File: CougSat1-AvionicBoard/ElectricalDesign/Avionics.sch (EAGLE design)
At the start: 0 parts

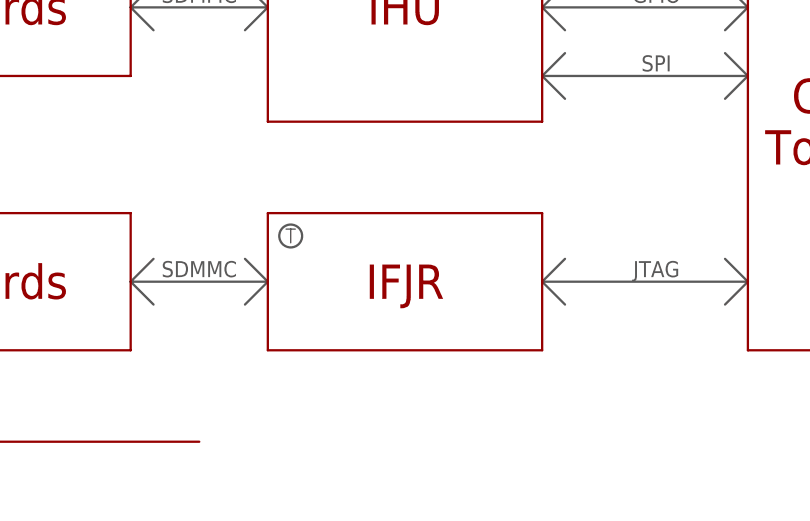
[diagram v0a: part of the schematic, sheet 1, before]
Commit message: Specified IFJR is a µController
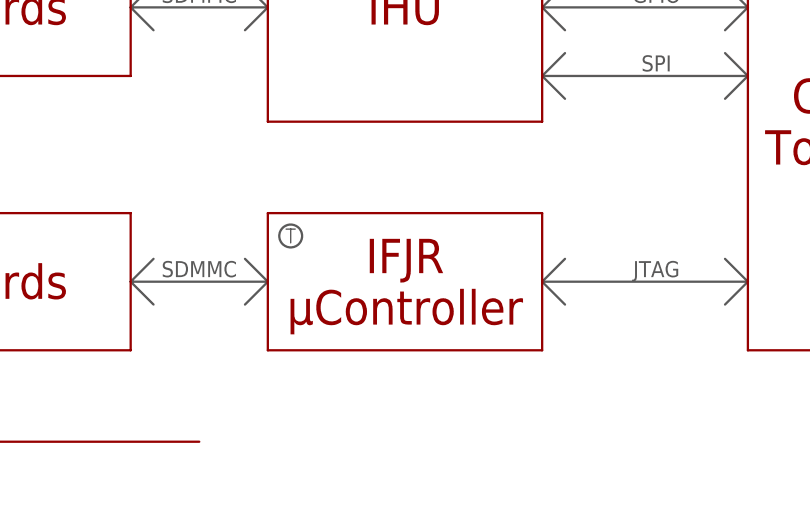
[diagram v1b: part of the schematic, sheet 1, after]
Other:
- note removed: "IFJR"
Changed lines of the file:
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@@
 <text x="215.9" y="60.96" size="3.81" layer="94" align="center">Connector:
 To Backplane</text>
-<text x="160.02" y="43.18" size="3.81" layer="94" align="center">IFJR</text>
+<text x="160.02" y="43.18" size="3.81" layer="94" align="center">IFJR
+µController</text>
 <text x="111.76" y="43.18" size="3.81" layer="94" align="center">SD Cards</text>
 <wire x1="198.12" y1="86.36" x2="233.68" y2="86.36" width="0.254" layer="94"/>

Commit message: Created Schematic for ADCS Portion
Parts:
- added C1, C2: 8pF ±0.25, CougsInSpace-Capacitors:CAP-V-8PF-1608
- added C10, C15: 1µF 10%, CougsInSpace-Capacitors:CAP-V-1UF-1608
- added C11, C12, C7, C8: 100nF 10%, CougsInSpace-Capacitors:CAP-V-100NF-1608
- added C13, C14: 15pF 1%, CougsInSpace-Capacitors:CAP-V-15PF-1608
- added C3: 10nF 10%, CougsInSpace-Capacitors:CAP-V-10NF-1608
- added C4: 10nF 10%, CougsInSpace-Capacitors:CAP-H-10NF-1608
- added C5: 100nF 10%, CougsInSpace-Capacitors:CAP-V-100NF-3216
- added C6: 6.8nF 5%, CougsInSpace-Capacitors:CAP-V-6.8NF-1608
- added D1: MBRM120LT, CougsInSpace-DiscreteSemi:DIODE-SCHOTTKY-H-POWERMITE
- added DS1: Green, CougsInSpace-LEDs:LED-V-GRN-1608
- added J1: (no value), CougsInSpace-Connectors:COAX-SMA-T-R
- added L1, L2, L3: xxx Turns, CougsInSpace-Coils:MAGNETORQUER-1UPV-SMD-3030
- added R1, R19, R2, R21, R3, R4: 0Ω <20mΩ, CougsInSpace-Resistors:RES-V-0-1608
- added R10, R11, R6, R7, R8, R9: 100mΩ 1%, CougsInSpace-Resistors:RES-H-0.1R-3216
- added R12, R14, R17: 33kΩ 1%, CougsInSpace-Resistors:RES-V-33K-1608
- added R13: 560Ω 1%, CougsInSpace-Resistors:RES-H-560R-1608
- added R15, R16: 8.45kΩ 0.1%, CougsInSpace-Resistors:RES-V-8.45K-1608
- added R18, R5: 0Ω <20mΩ, CougsInSpace-Resistors:RES-H-0-1608
- added R20, R22: 10kΩ 0.1%, CougsInSpace-Resistors:RES-V-10K-1608
- added RT1: 68kΩ 5%, CougsInSpace-Resistors:THERMISTOR-H-68K-1608
- added U10: BNO055, CougsInSpace-Sensors:BNO055
- added U2: STM32L476RGT, CougsInSpace-IC-µController:STM32-64P-L476RGT
- added U5, U6, U7: DRV8837, CougsInSpace-IC-Other:DRV8837
- added U8: LTC2499, CougsInSpace-IC-Conversion:LTC2499
- added U9: Venus838FLPx-L, CougsInSpace-RF:VENUS838FLPX
- added Y1: 16MHz ±10ppm, CougsInSpace-Clocks:CRYSTAL-16MHZ-SMD3.2X1.5
- added Y2: 32.768kHz ±10ppm, CougsInSpace-Clocks:CRYSTAL-32.768KHZ-SMD3.2X1.5
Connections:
- new net !NBOOT_LOAD_PIN: R22.2, U10.!BOOT_LOAD_PIN
- new net !NRESET: R20.1, U10.!RESET
- new net 3.3V: C7.1, U8.VCC
- new net 3.3V_2: C11.1, C12.1, D1.A, DS1.A, R12.2, U5.VCC, U6.VCC, U7.VCC, U9BASE.BOOT, U9BASE.VCC@1, U9BASE.VCC@2
- new net 5.0V: U5.VM, U6.VM, U7.VM
- new net ADCS_!WC: U2C.PC12
- new net ADCS_I2C_SCL: U2C.PC0, U8.SCL
- new net ADCS_I2C_SDA: U2C.PC1, U8.SDA
- new net ADCS_JDTO: U2B.PB3
- new net ADCS_JTCK: U2A.PA14
- new net ADCS_JTDI: U2A.PA15
- new net ADCS_JTMS: U2A.PA13
- new net AGND: J1.SHIELD, R15.2, R16.2, R2.1, R4.1, U8.COM, U8.REF-, U9BASE.RFGND
- new net AVDD: RT1.2
- new net AVREF: U8.REF+
- new net BUS_I2C0_IRQ: U2B.PB13
- new net BUS_I2C0_SCL: U2B.PB10
- new net BUS_I2C0_SDA: U2B.PB11
- new net CHASSIS: R3.1
- new net COIL-X_!SLEEP: U2B.PB4
- new net COIL-X_COIL+: L1.1, R7.2, U8.CH1
- new net COIL-X_IN1: U2B.PB9, U5.IN1
- new net COIL-X_IN2: U2B.PB8, U5.IN2
- new net COIL-X_OUT1: R6.1, U5.OUT1, U8.CH0
- new net COIL-X_SLEEP: U5.!SLEEP
- new net COIL-Y_!SLEEP: U2B.PB5
- new net COIL-Y_COIL+: L2.1, R9.2, U8.CH3
- new net COIL-Y_IN1: U2B.PB6, U6.IN1
- new net COIL-Y_IN2: U2B.PB7, U6.IN2
- new net COIL-Y_OUT1: R8.1, U6.OUT1, U8.CH2
- new net COIL-Y_SLEEP: U6.!SLEEP
- new net COIL-Z_!SLEEP: U2A.PA0
- new net COIL-Z_COIL+: L3.1, R11.2, U8.CH5
- new net COIL-Z_IN1: U2A.PA1, U7.IN1
- new net COIL-Z_IN2: U2A.PA2, U7.IN2
- new net COIL-Z_OUT1: R10.1, U7.OUT1, U8.CH4
- new net COIL-Z_SLEEP: U7.!SLEEP
- new net CTRL_RESET: R18.2
- new net DGND: C10.2, C11.2, C12.2, C13.2, C14.2, C15.2, C3.2, C4.1, C5.1, C6.2, C7.2, C8.2, R1.1, R20.2, R22.1, R5.1, U10.COM2, U10.DGND, U10.DGNDIO, U10.VDDIO, U2BASE.VSS@1, U2BASE.VSS@2, U2BASE.VSS@3, U2BASE.VSS@4, U2BASE.VSSA/VREF-, U8.CA0, U8.CA1, U8.CA2, U8.DGND, U8.F0, U9BASE.DGND, U9GPIO.GPIO1, U9GPIO.GPIO10, U9GPIO.GPIO11, U9GPIO.GPIO12, U9GPIO.GPIO13, U9GPIO.GPIO14, U9GPIO.GPIO15, U9GPIO.GPIO16, U9GPIO.GPIO2, U9GPIO.GPIO20, U9GPIO.GPIO21, U9GPIO.GPIO22, U9GPIO.GPIO23, U9GPIO.GPIO24, U9GPIO.GPIO25, U9GPIO.GPIO26, U9GPIO.GPIO27, U9GPIO.GPIO28, U9GPIO.GPIO29, U9GPIO.GPIO30, U9GPIO.GPIO31, U9GPIO.GPIO4, U9GPIO.GPIO5, U9GPIO.GPIO6, U9GPIO.GPIO7, U9GPIO.GPIO8, U9GPIO.GPIO9, Y1.GND
- new net GPS_!RESET: U2A.PA8
- new net GPS_LED: R13.1, U2B.PB12, U9BASE.LED
- new net GPS_PULSE: U2A.PA11, U9BASE.PULSE
- new net GPS_RESET: C10.1, R12.1, U9BASE.!RESET
- new net GPS_RX: U2A.PA10, U9BASE.TXD0
- new net GPS_TX: U2A.PA9, U9BASE.RXD0
- new net GPS_VBAT: C15.1, D1.C, U9BASE.VBAT
- new net I2C_ADDR_SEL: U10.COM3
- new net IMU_RESET: U2C.PC5
- new net INT: U10.INT
- new net N$1: C2.1, U2BASE.PH1-OSC_OUT, Y1.2
- new net N$10: R8.2, R9.1
- new net N$11: L2.2, U6.OUT2
- new net N$12: R10.2, R11.1
- new net N$13: R6.2, R7.1
- new net N$14: L3.2, U7.OUT2
- new net N$16: DS1.C, R13.2
- new net N$17: J1.CENTER, U9BASE.RFIN
- new net N$18: R16.1, R17.2, U8.ADCINP
- new net N$19: R14.1, U8.MUXOUTN
- new net N$2: C1.1, U2BASE.PH0-OSC_IN, Y1.1
- new net N$22: C13.1, U2C.PC14, Y2.1
- new net N$23: C14.1, U2C.PC15, Y2.2
- new net N$24: R17.1, U8.MUXOUTP
- new net N$25: R14.2, R15.1, U8.ADCINN
- new net N$27: U8.CH7
- new net N$28: U8.CH8
- new net N$3: R5.2, U2BASE.BOOT0
- new net N$4: C4.2, U10.CAP
- new net N$5: C1.2, C2.2
- new net N$6: C3.1, R18.1, U2BASE.!NRST
- new net N$8: C5.2, C6.1, C8.1, U10.VDD
- new net N$9: L1.2, U5.OUT2
- new net OPTIONAL_OSC_INPUT: U10.XIN32, U10.XOUT32
- new net PGND: R1.2, R2.2, R3.2, R4.2, U5.PGND, U6.PGND, U7.PGND
- new net PR_3.3V-2: U2BASE.VDD@1, U2BASE.VDD@2, U2BASE.VDD@3, U2BASE.VDDA/VREF+, U2BASE.VDDUSB
- new net PR_3.3V-3: R19.1, R21.1
- new net PS0: U10.PS0
- new net PS1: U10.PS1
- new net SCL: R19.2, U10.COM1
- new net SDA: R21.2, U10.COM0
- new net TEMP_GPS: RT1.1, U8.CH6
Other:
- note added: "3B1>"
- note added: "3B3>"
- note added: "5A2>"
- note added: "5A3>"
- note added: "5B2>"
- note added: "5B3>"
- note added: "5C2>"
- note added: "5C3>"
- note added: "6A2>"
- note added: "7B2>"
- note added: "7B3>"
- note added: "7C3>"
- note added: "<3B1"
- note added: "<3B4"
- note added: "<3B4>"
- note added: "<6B2"
- note added: "<7B3"
- note added: "<7C3"
- note added: "CAD Note: Decoupling"
- note added: "CAD Note: Thermally Connected"
- note removed: "SDMMC"

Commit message: Updated Avionics Schematic
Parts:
- added C16, C20, C21, C9: 8pF ±0.25, CougsInSpace-Capacitors:CAP-V-8PF-1608
- added C17, C18, C23, C24, C27, C28: 15pF 1%, CougsInSpace-Capacitors:CAP-V-15PF-1608
- added C19, C22: 10nF 10%, CougsInSpace-Capacitors:CAP-V-10NF-1608
- added C25, C26, C29, C30, C31: 100nF 10%, CougsInSpace-Capacitors:CAP-V-100NF-1608
- added J10, J16, J2, J6: (no value), CougsInSpace-Connectors:µSD-SW-PUSH-PUSH
- added J11, J12, J13, J14, J15, J5: (no value), CougsInSpace-Connectors:1X04-PICOLOCK
- added J3, J8, J9: SWD, CougsInSpace-Connectors:SWDSMD-6-R
- added J4, J7: CougSat Card, CougsInSpace-Boards:CIS_CARD-OPEN+X
- added R23, R24, R27, R28: 0Ω <20mΩ, CougsInSpace-Resistors:RES-H-0-1608
- added R25: 10kΩ 0.1%, CougsInSpace-Resistors:RES-V-10K-1608
- added R26, R36, R37, R38: 1kΩ 0.1%, CougsInSpace-Resistors:RES-V-1K-1608
- added R29, R30: 20kΩ 0.1%, CougsInSpace-Resistors:RES-V-PAIRED-20K-1616
- added R31: 20kΩ 0.1%, CougsInSpace-Resistors:RES-H-PAIRED-20K-1616
- added R33, R34, R35: 1kΩ 0.1%, CougsInSpace-Resistors:RES-H-1K-1608
- added RT2, RT3, RT4, RT5, RT6, RT7: 68kΩ 5%, CougsInSpace-Resistors:THERMISTOR-H-68K-1608
- added U1, U3: STM32L476RGT, CougsInSpace-IC-µController:STM32-64P-L476RGT
- added U11, U4: 128KB, CougsInSpace-IC-Memory:EEPROM-I2C-4-128KB-SO8
- added U12, U13: TXS0102DQM, CougsInSpace-IC-Logic:LEVEL_SHIFTER-2BIT-XSON-8
- added U14: LTC2499, CougsInSpace-IC-Conversion:LTC2499
- added Y3, Y5: 16MHz ±10ppm, CougsInSpace-Clocks:CRYSTAL-16MHZ-SMD3.2X1.5
- added Y4, Y6, Y7: 32.768kHz ±10ppm, CougsInSpace-Clocks:CRYSTAL-32.768KHZ-SMD3.2X1.5
- R14: value 33kΩ 1% -> 20kΩ 0.1%; device CougsInSpace-Resistors:RES-V-33K-1608 -> CougsInSpace-Resistors:RES-V-PAIRED-20K-1616
- R15: value 8.45kΩ 0.1% -> 20kΩ 0.1%; device CougsInSpace-Resistors:RES-V-8.45K-1608 -> CougsInSpace-Resistors:RES-V-PAIRED-20K-1616
- R16: value 8.45kΩ 0.1% -> 20kΩ 0.1%; device CougsInSpace-Resistors:RES-V-8.45K-1608 -> CougsInSpace-Resistors:RES-H-PAIRED-20K-1616
- R17: value 33kΩ 1% -> 20kΩ 0.1%; device CougsInSpace-Resistors:RES-V-33K-1608 -> CougsInSpace-Resistors:RES-H-PAIRED-20K-1616
- R19, R21: value 0Ω <20mΩ -> 1kΩ 0.1%; device CougsInSpace-Resistors:RES-V-0-1608 -> CougsInSpace-Resistors:RES-V-1K-1608
- R22: value 10kΩ 0.1% -> 1kΩ 0.1%; device CougsInSpace-Resistors:RES-V-10K-1608 -> CougsInSpace-Resistors:RES-V-1K-1608
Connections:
- net !NRESET renamed !IMU_RESET
- net INT renamed IMU0_INT
- net N$27 renamed TEMP_IMU
- removed net !NBOOT_LOAD_PIN: R22.2, U10.!BOOT_LOAD_PIN
- removed net 5.0V: U5.VM, U6.VM, U7.VM
- removed net ADCS_I2C_SCL: U2C.PC0, U8.SCL
- removed net ADCS_I2C_SDA: U2C.PC1, U8.SDA
- removed net I2C_ADDR_SEL: U10.COM3
- removed net OPTIONAL_OSC_INPUT: U10.XIN32, U10.XOUT32
- removed net PR_3.3V-2: U2BASE.VDD@1, U2BASE.VDD@2, U2BASE.VDD@3, U2BASE.VDDA/VREF+, U2BASE.VDDUSB
- removed net PR_3.3V-3: R19.1, R21.1
- removed net PS0: U10.PS0
- removed net PS1: U10.PS1
- removed net SCL: R19.2, U10.COM1
- removed net SDA: R21.2, U10.COM0
- new net !IMU0_BOOT-A: R25.2, U10.!BOOT_LOAD_PIN
- new net 3.3V_0: J7POWER.PR_3.3V-0, R35.2, R38.2, U3BASE.VBAT, U3BASE.VDD@1, U3BASE.VDD@2, U3BASE.VDD@3, U3BASE.VDDUSB
- new net 3.3V_1: J7POWER.PR_3.3V-1
- new net 3.3V_3: C5.2, C6.2, C8.2, R20.2, R25.1, U10.VDD, U10.VDDIO
- new net 3.3V_4: C11.1, C12.1, D1.A, DS1.A, R12.2, U9BASE.BOOT, U9BASE.VCC@1, U9BASE.VCC@2
- new net 3.3V_5: J10.VDD, J16.VDD, J2.VDD, J6.VDD, R34.2, R37.2, U12.VCCB, U13.VCCB
- new net 3.3V_6: C25.1, C26.1, C30.1, C31.1
- new net ADCS_!RESET: J3.!RST
- new net ADCS_I2C0_SCL: R26.1, U10.COM1, U11.SDA, U2B.PB6, U4.SDA, U8.SCL
- new net ADCS_I2C0_SDA: R22.1, U10.COM0, U11.SCL, U2B.PB7, U4.SCL, U8.SDA
- new net ADCS_I2C1_SCL: R21.1, U2C.PC0
- new net ADCS_I2C1_SDA: R19.1, U2C.PC1
- new net ADCS_JTDO: J3.SWO, U13.A1
- new net ADC_COIL-X_COIL+: R16.A2, U8.CH1
- new net ADC_COIL-X_OUT1: R16.B2, U8.CH0
- new net ADC_COIL-Y_COIL+: R17.A2, U8.CH3
- new net ADC_COIL-Y_OUT1: R17.B2, U8.CH2
- new net ADC_COIL-Z_COIL+: R31.A2, U8.CH5
- new net ADC_COIL-Z_OUT1: R31.B2, U8.CH4
- new net BUS_I2C1_IRQ: J4DATA.BUS_I2C1_IRQ, U3B.PB12
- new net BUS_I2C1_SCL: J4DATA.BUS_I2C1_SCL, U3B.PB13
- new net BUS_I2C1_SDA: J4DATA.BUS_I2C1_SDA, U3B.PB11
- new net BUS_JTAG_TCK: J4JTAG.BUS_JTAG_TCK, U12.B1, U1A.PA0
- new net BUS_JTAG_TDI: J4JTAG.BUS_JTAG_TDI, U12.B2, U1A.PA1
- new net BUS_JTAG_TDO: J4JTAG.BUS_JTAG_TDO, U13.B1, U1A.PA2
- new net BUS_JTAG_TMS: J4JTAG.BUS_JTAG_TMS, U13.B2, U1A.PA3
- new net CTRL_!RESET: J4DATA.CTRL_!RESET
- new net CTRL_SYNC: J4DATA.CTRL_SYNC
- new net EEPROM0_WC: U2C.PC6, U4.!WC
- new net EEPROM1_WC: U11.!WC, U2C.PC7
- new net I2C_SCL: J11.3, J12.3, J13.3, J14.3, J15.3, J5.3
- new net I2C_SDA: J11.2, J12.2, J13.2, J14.2, J15.2, J5.2
- new net IFJR_!RESET: J8.!RST
- new net IFJR_JDTI: U1A.PA15
- new net IFJR_JTCK: J8.SWCLK, U1A.PA14
- new net IFJR_JTDO: J8.SWO, U1B.PB3
- new net IFJR_JTMS: J8.SWDIO, U1A.PA13
- new net IHU_!RESET: J9.!RST
- new net IHU_GPIO-0: J4GPIO.GPIO-0, U3A.PA0
- new net IHU_GPIO-1: J4GPIO.GPIO-1, U3A.PA1
- new net IHU_GPIO-2: J4GPIO.GPIO-2, U3A.PA2
- new net IHU_GPIO-3: J4GPIO.GPIO-3, U3A.PA3
- new net IHU_GPIO-4: J4GPIO.GPIO-4, U3A.PA4
- new net IHU_GPIO-5: J4GPIO.GPIO-5, U3A.PA8
- new net IHU_GPIO-6: J4GPIO.GPIO-6, U3A.PA9
- new net IHU_GPIO-7: J4GPIO.GPIO-7, U3A.PA10
- new net IHU_GPIO-8: J4GPIO.GPIO-8, U3A.PA11
- new net IHU_GPIO-9: J4GPIO.GPIO-9, U3A.PA12
- new net IHU_JTCK: J9.SWCLK
- new net IHU_JTDO: J9.SWO
- new net IHU_JTMS: J9.SWDIO
- new net JTAG_OE: J4JTAG.BUS_JTAG_EN-0, U12.OE, U13.OE, U1C.PC3
- new net N$15: C16.1, U1BASE.PH1-OSC_OUT, Y3.2
- new net N$21: R23.2, U1BASE.BOOT0
- new net N$26: C17.1, U1C.PC14, Y4.1
- new net N$27: R29.B2, U14.MUXOUTN
- new net N$29: C18.1, U1C.PC15, Y4.2
- new net N$30: C19.1, R24.1, U1BASE.!NRST
- new net N$31: C20.2, C21.2
- new net N$32: R27.2, U3BASE.BOOT0
- new net N$33: J16.CD/DAT3
- new net N$34: C20.1, U3BASE.PH0-OSC_IN, Y5.1
- new net N$35: C22.1, R28.1, U3BASE.!NRST
- new net N$36: C23.1, U3C.PC14, Y6.1
- new net N$37: C27.1, U10.XOUT32, Y7.1
- new net N$38: C24.1, U3C.PC15, Y6.2
- new net N$39: C4.1
- new net N$40: J6.CD/DAT3
- new net N$41: J2.CMD, J6.CMD
- new net N$42: U1BASE.VBAT, U1BASE.VDD@1, U1BASE.VDD@2, U1BASE.VDD@3, U1BASE.VDDUSB
- new net N$43: J2.CLK, J6.CLK
- new net N$44: C28.1, U10.XIN32, Y7.2
- new net N$45: J2.DAT0, J6.DAT0
- new net N$46: J6.SW+
- new net N$47: J2.CD/DAT3
- new net N$50: J2.SW+
- new net N$51: R29.B1, R30.B2, U14.ADCINN
- new net N$52: J7POWER.PR_3.3V-3
- new net N$53: J7POWER.PR_3.3V-4
- new net N$54: J7POWER.PR_3.3V-5
- new net N$55: J10.CMD, J16.CMD
- new net N$56: J10.CLK, J16.CLK
- new net N$57: J10.DAT0, J16.DAT0
- new net N$58: R33.1, U2BASE.VDDA/VREF+
- new net N$59: R34.1, U1BASE.VDDA/VREF+
- new net N$60: R35.1, U3BASE.VDDA/VREF+
- new net N$61: J3.VSENSE, R36.1
- new net N$62: J8.VSENSE, R37.1
- new net N$64: J9.VSENSE, R38.1
- new net N$65: R29.A1, R30.A2, U14.ADCINP
- new net N$7: C21.1, U3BASE.PH1-OSC_OUT, Y5.2
- new net N$70: J16.SW+
- new net N$71: J10.CD/DAT3
- new net N$72: J10.SW+
- new net SPI1_MISO: J4DATA.BUS_SPI_MISO, U1A.PA6, U3A.PA6
- new net SPI1_MOSI: J4DATA.BUS_SPI_MOSI, U1A.PA7, U3A.PA7
- new net SPI1_SCK: J4DATA.BUS_SPI_SCK, U1A.PA5, U3A.PA5
- new net SPI2_MISO: U3C.PC2
- new net SPI2_MOSI: U3C.PC3
- new net SPI2_SCK: U3B.PB10
- new net SPI3_MISO: U3C.PC11
- new net SPI3_MOSI: U3C.PC12
- new net SPI3_SCK: U3C.PC10
- new net SYS_JTCK-SWCLK: U3A.PA14
- new net SYS_JTDI: U3A.PA15
- new net SYS_JTDO-SWO: U3B.PB3
- new net SYS_JTMS-SWDIO: U3A.PA13
- new net TEMP_ADCS: U8.CH9
- new net TEMP_H-BRIDGE-X: RT3.1, U8.CH10
- new net TEMP_H-BRIDGE-Y: RT4.1, U8.CH11
- new net TEMP_H-BRIDGE-Z: RT5.1, U8.CH12
- new net TEMP_IFJR: RT2.1, U14.CH1
- new net TEMP_IHU: U14.CH0
- new net TEMP_SD_IFJR0: RT6.1, U14.CH4
- new net TEMP_SD_IFJR1: RT7.1, U14.CH5
- new net TEMP_SD_IHU0: U14.CH2
- new net TEMP_SD_IHU1: U14.CH3
- new net VBATT_5: J7POWER.PR_BATT-5, U5.VM, U6.VM, U7.VM
- net 3.3V: now also C29.1, J11.1, J12.1, J13.1, J14.1, J15.1, J5.1, U14.VCC
- net 3.3V_2: now also J7POWER.PR_3.3V-2, R33.2, R36.2, U11.E1, U11.VCC, U12.VCCA, U13.VCCA, U2BASE.VBAT, U2BASE.VDD@1, U2BASE.VDD@2, U2BASE.VDD@3, U2BASE.VDDUSB, U4.VCC; no longer C11.1, C12.1, D1.A, DS1.A, R12.2, U9BASE.BOOT, U9BASE.VCC@1, U9BASE.VCC@2
- net ADCS_!WC: now also U2C.PC4; no longer U2C.PC12
- net ADCS_JTCK: now also J3.SWCLK, U12.A1
- net ADCS_JTDI: now also U12.A2
- net ADCS_JTMS: now also J3.SWDIO, U13.A2
- net AGND: now also R15.A1, R15.B1, R30.A1, R30.B1, U14.COM, U14.REF-; no longer R15.2, R16.2
- net AVDD: now also RT2.2, RT3.2, RT4.2, RT5.2, RT6.2, RT7.2, U14.REF+, U8.REF+
- net AVREF: now also U14.CH8, U8.CH8; no longer U8.REF+
- net BUS_I2C0_IRQ: now also J4DATA.BUS_I2C0_IRQ, U2B.PB12, U3B.PB8; no longer U2B.PB13
- net BUS_I2C0_SCL: now also J4DATA.BUS_I2C0_SCL, U3B.PB6
- net BUS_I2C0_SDA: now also J4DATA.BUS_I2C0_SDA, U3B.PB7
- net CHASSIS: now also J7POWER.CHASSIS
- net COIL-X_!SLEEP: now also U2A.PA4; no longer U2B.PB4
- net COIL-X_COIL+: now also R16.A1; no longer U8.CH1
- net COIL-X_IN1: now also U2A.PA0; no longer U2B.PB9
- net COIL-X_IN2: now also U2A.PA1; no longer U2B.PB8
- net COIL-X_OUT1: now also R16.B1; no longer U8.CH0
- net COIL-Y_!SLEEP: now also U2A.PA5; no longer U2B.PB5
- net COIL-Y_COIL+: now also R17.A1; no longer U8.CH3
- net COIL-Y_IN1: now also U2A.PA2; no longer U2B.PB6
- net COIL-Y_IN2: now also U2A.PA3; no longer U2B.PB7
- net COIL-Y_OUT1: now also R17.B1; no longer U8.CH2
- net COIL-Z_!SLEEP: now also U2A.PA12; no longer U2A.PA0
- net COIL-Z_COIL+: now also R31.A1; no longer U8.CH5
- net COIL-Z_IN1: now also U2A.PA8; no longer U2A.PA1
- net COIL-Z_IN2: now also U2A.PA11; no longer U2A.PA2
- net COIL-Z_OUT1: now also R31.B1; no longer U8.CH4
- net CTRL_RESET: now also R24.2, R28.2
- net DGND: now also C16.2, C17.2, C18.2, C19.2, C22.2, C23.2, C24.2, C25.2, C26.2, C27.2, C28.2, C29.2, C30.2, C31.2, C6.1, C8.1, C9.2, J10.SW-, J10.VSS, J11.4, J12.4, J13.4, J14.4, J15.4, J16.SW-, J16.VSS, J2.SW-, J2.VSS, J3.DGND, J5.4, J6.SW-, J6.VSS, J8.DGND, J9.DGND, R23.1, R27.1, U10.COM3, U10.PS0, U10.PS1, U11.DGND, U11.E2, U12.DGND, U13.DGND, U14.CA0, U14.CA1, U14.CA2, U14.DGND, U14.F0, U1BASE.VSS@1, U1BASE.VSS@2, U1BASE.VSS@3, U1BASE.VSS@4, U1BASE.VSSA/VREF-, U3BASE.VSS@1, U3BASE.VSS@2, U3BASE.VSS@3, U3BASE.VSS@4, U3BASE.VSSA/VREF-, U4.DGND, U4.E1, U4.E2, Y3.GND, Y5.GND; no longer C4.1, C6.2, C8.2, R20.2, R22.1, U10.VDDIO
- net GPS_!RESET: now also U2A.PA6; no longer U2A.PA8
- net GPS_LED: now also U2B.PB0; no longer U2B.PB12
- net GPS_PULSE: now also U2A.PA7; no longer U2A.PA11
- net IMU_RESET: now also U2C.PC3; no longer U2C.PC5
- net N$18: now also R14.B1, R15.B2, U8.ADCINN; no longer R16.1, R17.2, U8.ADCINP
- net N$19: now also R14.A1, R15.A2, U8.ADCINP; no longer R14.1, U8.MUXOUTN
- net N$22: no longer U2C.PC14
- net N$24: now also R14.B2, U8.MUXOUTN; no longer R17.1, U8.MUXOUTP
- net N$25: now also R14.A2, U8.MUXOUTP; no longer R14.2, R15.1, U8.ADCINN
- net N$28: now also R29.A2, U14.MUXOUTP; no longer U8.CH8
- net N$8: now also C9.1, U1BASE.PH0-OSC_IN, Y3.1; no longer C5.2, C6.1, C8.1, U10.VDD
- net PGND: now also J7POWER.PGND
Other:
- note added: "3B2>"
- note added: "3B6>"
- note added: "3C2> 3D2>"
- note added: "5A1>"
- note added: "5B1>"
- note added: "5C1>"
- note added: "7B1>"
- note added: "<3B2"
- note added: "<3B3"
- note added: "<3B3>"
- note added: "<3B6"
- note added: "<3B6>"
- note added: "<3C1"
- note removed: "3B1>"
- note removed: "5A2>"
- note removed: "5A3>"
- note removed: "5B2>"
- note removed: "5B3>"
- note removed: "5C2>"
- note removed: "5C3>"
- note removed: "6A2>"
- note removed: "7B3>"
- note removed: "7C3>"
- note removed: "<3B1"
- note removed: "<3B4"
- note removed: "<3B4>"
- note removed: "<7C3"
